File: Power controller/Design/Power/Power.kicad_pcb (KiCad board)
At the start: 2 copper layers, 34 parts, among them IC1 MP2307DN-LF-Z, IC2 MAX17261METD+, J1 Conn_01x02, J2 Conn_02x03_Odd_Even, J3 Conn_01x02, Q1 IRF7403, Q2 IRF7403, Q3 IRF7403, U1 ATmega328PB-MU, U2 MCP1415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

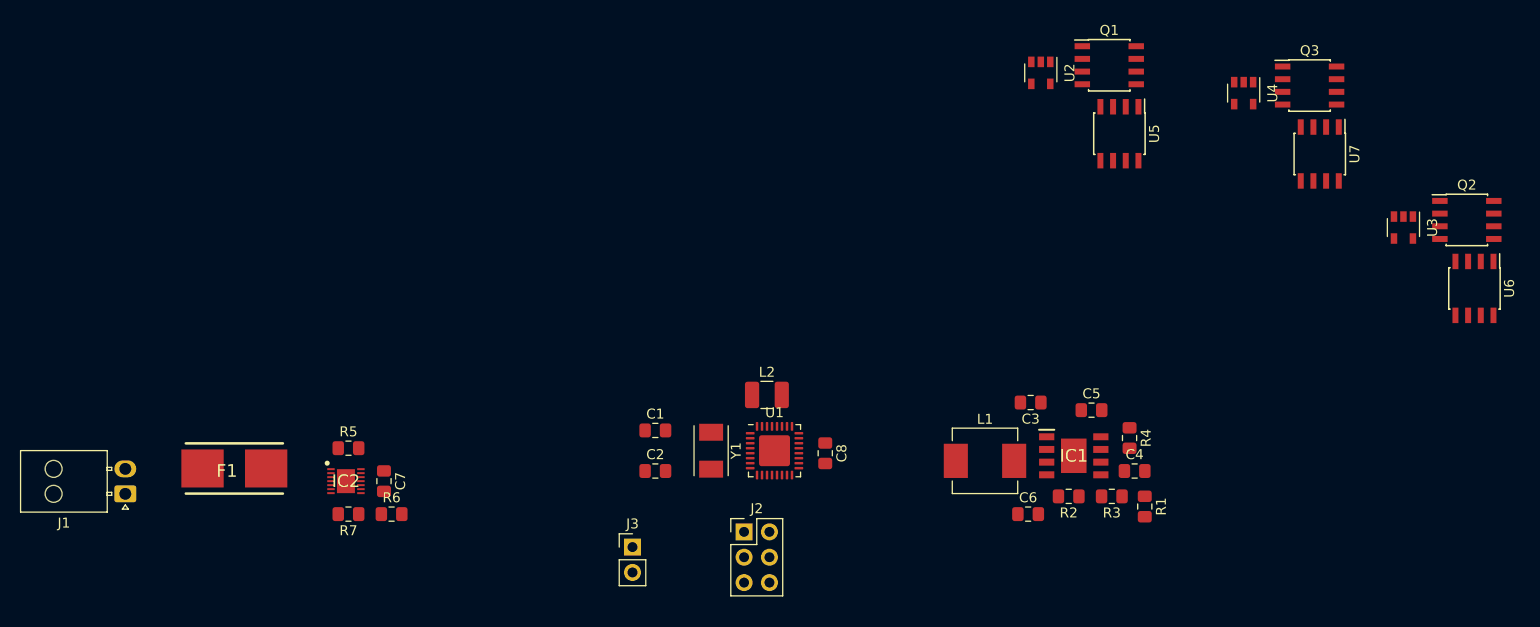
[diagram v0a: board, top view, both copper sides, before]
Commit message: Removed fuel gauge, grouped PCB
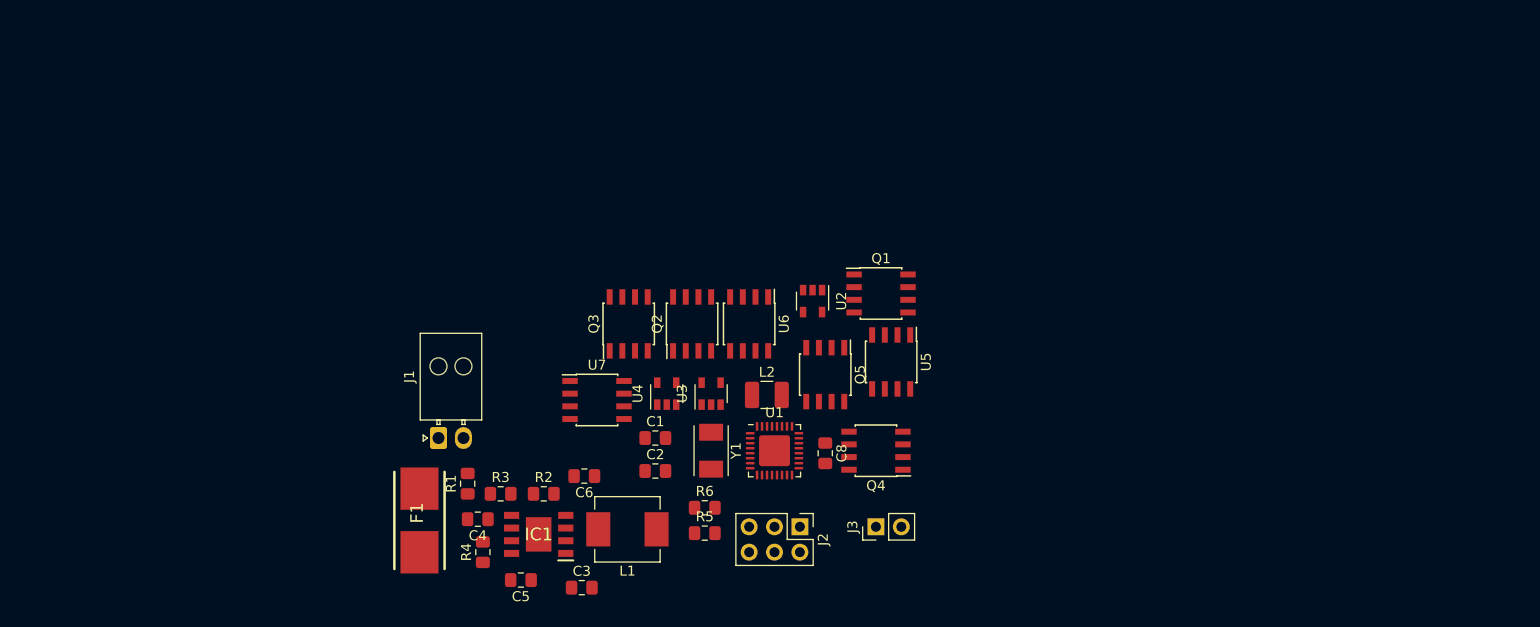
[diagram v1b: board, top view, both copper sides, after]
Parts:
- removed C7: 0.47u, Capacitor_SMD:C_0805_2012Metric_Pad1.15x1.40mm_HandSolder
- removed IC2: MAX17261METD+, SamacSys_Parts:SON40P300X300X80-15N
- removed R7: 200k, Resistor_SMD:R_0805_2012Metric_Pad1.15x1.40mm_HandSolder
- added Q4: IRF7403, Package_SO:SOIC-8_3.9x4.9mm_P1.27mm, F.Cu at (134.6, 62.2)
- added Q5: IRF7403, Package_SO:SOIC-8_3.9x4.9mm_P1.27mm, F.Cu at (129.5, 54.6)
- R5: value 5m -> 4k7
- R6: value 1.8M -> 4k7
- moved Q2 78.3 mm to (116.2, 49.5), turned to 90 degrees
- moved U7 76.5 mm to (106.7, 57.1), turned to 0 degrees
- moved U6 72.7 mm to (121.9, 49.5)
- moved Q3 72.3 mm to (109.9, 49.5), turned to 90 degrees
- moved U3 71.3 mm to (118.1, 56.5), turned to 90 degrees
- moved R1 67.9 mm to (93.7, 65.5), turned to 90 degrees
- moved C4 66.0 mm to (94.7, 69.1), turned to 180 degrees
- moved R4 65.8 mm to (95.2, 72.4), turned to 90 degrees
- moved U4 65.2 mm to (113.7, 56.5), turned to 90 degrees
- moved R3 61.2 mm to (97.0, 66.5), turned to 0 degrees
- moved C5 59.6 mm to (99.1, 75.2), turned to 180 degrees
- moved IC1 54.2 mm to (100.8, 70.6), turned to 180 degrees
- moved R2 52.6 mm to (101.3, 66.5), turned to 0 degrees
- moved C3 48.6 mm to (105.2, 75.9), turned to 0 degrees
- moved C6 44.6 mm to (105.4, 64.8), turned to 180 degrees
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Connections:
- R5 pad 1: GND -> SDA
- R5 pad 2: Net-(IC2-Pad15) -> 5V
- R6 pad 1: Net-(IC2-Pad10) -> SCL
- R6 pad 2: VBAT -> 5V
- U1 pad 27: Net-(U1-Pad27) -> SDA
- U1 pad 28: Net-(U1-Pad28) -> SCL
